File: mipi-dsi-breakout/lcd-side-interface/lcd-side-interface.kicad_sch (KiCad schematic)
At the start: 5 parts

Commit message: Add symbols for the rest of the lcd screens.
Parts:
- removed S1: ~, symbol project:et060hd02_t_dsi_conn
- removed U1: ~, symbol project:tst043wvbi_130c_ctp_conn
- removed U2: ~, symbol project:et050fw04_t_dsi_conn
- removed X1: ~, symbol project:mipi_breakout_header_conn
- removed Y1: ~, symbol project:tst043wvbi_130c_dsi_conn

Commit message: Layout schematic for lcd side interface.
Also change most pins on the mipi 20 pin header interface connector to
bidirectional to avoid ERC headache.
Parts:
- added H1: MountingHole_Pad, symbol Mechanical:MountingHole_Pad
- added X1: ~, symbol project:mipi_breakout_header_conn
- added et050fw04_t_dsi1: ~, symbol project:et050fw04_t_dsi_conn
- added et060hd02_t_dsi1: ~, symbol project:et060hd02_t_dsi_conn
- added tst043wvbi_130c_ctp1: ~, symbol project:tst043wvbi_130c_ctp_conn
- added tst043wvbi_130c_dsi1: ~, symbol project:tst043wvbi_130c_dsi_conn
- added tst050hdbs_80c_ctp1: ~, symbol project:tst050hdbs_80c_ctp_conn
- added tst050hdbs_80c_dsi1: ~, symbol project:tst050hdbs_80c_dsi_conn
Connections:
- new net +1V8: X1.2 (VCC1.8), et050fw04_t_dsi1.18 (IOVCC_1.8V), et050fw04_t_dsi1.19 (IOVCC_1.8V), et060hd02_t_dsi1.18 (IOVCC), tst043wvbi_130c_dsi1.7 (IOVCC), tst050hdbs_80c_ctp1.2 (VDDIO), tst050hdbs_80c_dsi1.8 (IOVCC)
- new net DSI_0_N: X1.11 (DSI_0_N), et050fw04_t_dsi1.3 (MIPI_0N), et060hd02_t_dsi1.13 (TD0N), tst043wvbi_130c_dsi1.15 (MIPI_D0_N), tst050hdbs_80c_dsi1.13 (D0N)
- new net DSI_0_P: X1.12 (DSI_0_P), et050fw04_t_dsi1.2 (MIPI_0P), et060hd02_t_dsi1.14 (TD0P), tst043wvbi_130c_dsi1.16 (MIPI_D0_P), tst050hdbs_80c_dsi1.14 (D0P)
- new net DSI_1_N: X1.13 (DSI_1_N), et050fw04_t_dsi1.6 (MIPI_1N), et060hd02_t_dsi1.10 (TD1N), tst043wvbi_130c_dsi1.13 (MIPI_D1_N), tst050hdbs_80c_dsi1.16 (D1N)
- new net DSI_1_P: X1.14 (DSI_1_P), et050fw04_t_dsi1.5 (MIPI_1P), et060hd02_t_dsi1.11 (TD1P), tst043wvbi_130c_dsi1.12 (MIPI_D1_P), tst050hdbs_80c_dsi1.17 (D1P)
- new net DSI_2_N: X1.17 (DSI_2_N), et060hd02_t_dsi1.4 (TD2N), tst050hdbs_80c_dsi1.22 (D2N)
- new net DSI_2_P: X1.18 (DSI_2_P), et060hd02_t_dsi1.5 (TD2P), tst050hdbs_80c_dsi1.23 (D2P)
- new net DSI_3_N: X1.19 (DSI_3_N), et060hd02_t_dsi1.1 (TD3N), tst050hdbs_80c_dsi1.25 (D3N)
- new net DSI_3_P: X1.20 (DSI_3_P), et060hd02_t_dsi1.2 (TD3P), tst050hdbs_80c_dsi1.26 (D3P)
- new net DSI_CLK_N: X1.15 (DSI_CLK_N), et050fw04_t_dsi1.9 (MIPI_CKN), et060hd02_t_dsi1.7 (TCN), tst043wvbi_130c_dsi1.19 (MIPI_CLK_N), tst050hdbs_80c_dsi1.19 (CLKN)
- new net DSI_CLK_P: X1.16 (DSI_CLK_P), et050fw04_t_dsi1.8 (MIPI_CKP), et060hd02_t_dsi1.8 (TCP), tst043wvbi_130c_dsi1.18 (MIPI_CLK_P), tst050hdbs_80c_dsi1.20 (CLKP)
- new net GND: H1.1, X1.3 (GND), et050fw04_t_dsi1.1 (GND), et050fw04_t_dsi1.10 (GND), et050fw04_t_dsi1.13 (GND), et050fw04_t_dsi1.16 (GND), et050fw04_t_dsi1.17 (GND), et050fw04_t_dsi1.27 (GND), et050fw04_t_dsi1.30 (GND), et050fw04_t_dsi1.32 (GND), et050fw04_t_dsi1.33 (GND), et050fw04_t_dsi1.37 (GND), et050fw04_t_dsi1.4 (GND), et050fw04_t_dsi1.7 (GND), et060hd02_t_dsi1.12 (GND), et060hd02_t_dsi1.15 (GND), et060hd02_t_dsi1.19 (GND), et060hd02_t_dsi1.3 (GND), et060hd02_t_dsi1.6 (GND), et060hd02_t_dsi1.9 (GND), tst043wvbi_130c_ctp1.4 (GND), tst043wvbi_130c_ctp1.8 (GND), tst043wvbi_130c_ctp1.9 (GND), tst043wvbi_130c_dsi1.11 (GND), tst043wvbi_130c_dsi1.14 (GND), tst043wvbi_130c_dsi1.17 (GND), tst043wvbi_130c_dsi1.8 (GND), tst050hdbs_80c_ctp1.1 (GND), tst050hdbs_80c_ctp1.8 (GND), tst050hdbs_80c_dsi1.12 (GND), tst050hdbs_80c_dsi1.15 (GND), tst050hdbs_80c_dsi1.18 (GND), tst050hdbs_80c_dsi1.21 (GND), tst050hdbs_80c_dsi1.24 (GND), tst050hdbs_80c_dsi1.27 (GND), tst050hdbs_80c_dsi1.28 (GND), tst050hdbs_80c_dsi1.6 (GND)
- new net INT: X1.5 (INTERRUPT), tst043wvbi_130c_ctp1.5 (Interrupt), tst050hdbs_80c_ctp1.6 (INT)
- new net LED_A: X1.9 (LED_A), et050fw04_t_dsi1.35 (LED_A), et050fw04_t_dsi1.36 (LED_A), et060hd02_t_dsi1.24 (LEDA), et060hd02_t_dsi1.25 (LEDA), tst043wvbi_130c_dsi1.1 (LED_A), tst043wvbi_130c_dsi1.2 (LED_A), tst050hdbs_80c_dsi1.2 (LEDA), tst050hdbs_80c_dsi1.3 (LEDA)
- new net LED_K: X1.10 (LED_K), et050fw04_t_dsi1.28 (LED_K), et050fw04_t_dsi1.29 (LED_K), et060hd02_t_dsi1.21 (LEDK), et060hd02_t_dsi1.22 (LEDK), tst043wvbi_130c_dsi1.3 (LED_K), tst043wvbi_130c_dsi1.4 (LED_K), tst050hdbs_80c_dsi1.4 (LEDK), tst050hdbs_80c_dsi1.5 (LEDK)
- new net RESET: X1.4 (RESET_N), et050fw04_t_dsi1.24 (RESET), et060hd02_t_dsi1.16 (RESET), tst043wvbi_130c_ctp1.3 (Reset), tst043wvbi_130c_dsi1.10 (LCD_RST_N), tst050hdbs_80c_ctp1.7 (RST), tst050hdbs_80c_dsi1.11 (RESET_B)
- new net SCL: X1.7 (SCL), tst043wvbi_130c_ctp1.7 (SCL), tst050hdbs_80c_ctp1.4 (SCL)
- new net SDA: X1.8 (SDA), tst043wvbi_130c_ctp1.6 (SDA), tst050hdbs_80c_ctp1.5 (SDA)
- new net TE_O: X1.6 (TE_O), et050fw04_t_dsi1.20 (TE), tst043wvbi_130c_dsi1.9 (LCD_TEO), tst050hdbs_80c_dsi1.10 (TE)
- new net VCC: X1.1 (VCC), et050fw04_t_dsi1.38 (VCC_2.8V), et050fw04_t_dsi1.39 (VCC_2.8V), et060hd02_t_dsi1.17 (VCC), tst043wvbi_130c_ctp1.10 (VDD), tst043wvbi_130c_dsi1.6 (VCC), tst050hdbs_80c_ctp1.3 (VDD), tst050hdbs_80c_dsi1.7 (VCC2.8V)
- no-connect marks 0 -> 2
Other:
- note added: "Exposed ground pad (no through hole) for grounding SUS cable stiffeners. (This is meant to be connected using flexible conductive tape.)"

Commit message: Hook up step models to footprints.
Also add new footprint for sus grounding pad.
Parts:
- H1: footprint (none) -> project:sus-grounding-pad
- X1: footprint (none) -> Connector_PinHeader_2.54mm:PinHeader_1x20_P2.54mm_Horizontal
- et050fw04_t_dsi1: footprint (none) -> project:Cvilux_CF4240FH0R0-05-NH_40pos-0.5mm-zif
- et060hd02_t_dsi1: footprint (none) -> project:Cvilux_CF5825DH0RA-NH_25pos-0.3mm-zif
- tst043wvbi_130c_ctp1: footprint (none) -> project:TE_1-2328702-0_10pos-0.5mm-zif
- tst043wvbi_130c_dsi1: footprint (none) -> project:Cvilux_CF4220FH0R0-05-NH_20pos-0.5mm-zif
- tst050hdbs_80c_ctp1: footprint (none) -> project:TE_2328702_8pos-0.5mm-zif
- tst050hdbs_80c_dsi1: footprint (none) -> project:Cvilux_CF4230FH0R0-05-NH_30pos-0.5mm-zif
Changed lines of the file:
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@@
 			)
 		)
-		(property "Footprint" ""
+		(property "Footprint" "project:sus-grounding-pad"
 			(at 193.04 144.78 0)
 			(effects
@@
 			)
 		)
-		(property "Footprint" ""
+		(property "Footprint" "project:TE_2328702_8pos-0.5mm-zif"
 			(at 113.03 63.5 0)
 			(effects
@@
 			)
 		)
-		(property "Footprint" ""
+		(property "Footprint" "project:TE_1-2328702-0_10pos-0.5mm-zif"
 			(at 113.03 106.68 0)
 			(effects
@@
 			)
 		)
-		(property "Footprint" ""
+		(property "Footprint" "project:Cvilux_CF4230FH0R0-05-NH_30pos-0.5mm-zif"
 			(at 168.91 86.36 0)
 			(effects
@@
 			)
 		)
-		(property "Footprint" ""
+		(property "Footprint" "project:Cvilux_CF5825DH0RA-NH_25pos-0.3mm-zif"
 			(at 80.01 86.36 0)
 			(effects
@@
 			)
 		)
-		(property "Footprint" ""
+		(property "Footprint" "Connector_PinHeader_2.54mm:PinHeader_1x20_P2.54mm_Horizontal"
 			(at 146.05 157.48 0)
 			(effects
@@
 			)
 		)
-		(property "Footprint" ""
+		(property "Footprint" "project:Cvilux_CF4240FH0R0-05-NH_40pos-0.5mm-zif"
 			(at 219.71 80.01 0)
 			(effects
@@
 			)
 		)
-		(property "Footprint" ""
+		(property "Footprint" "project:Cvilux_CF4220FH0R0-05-NH_20pos-0.5mm-zif"
 			(at 83.82 158.75 0)
 			(effects

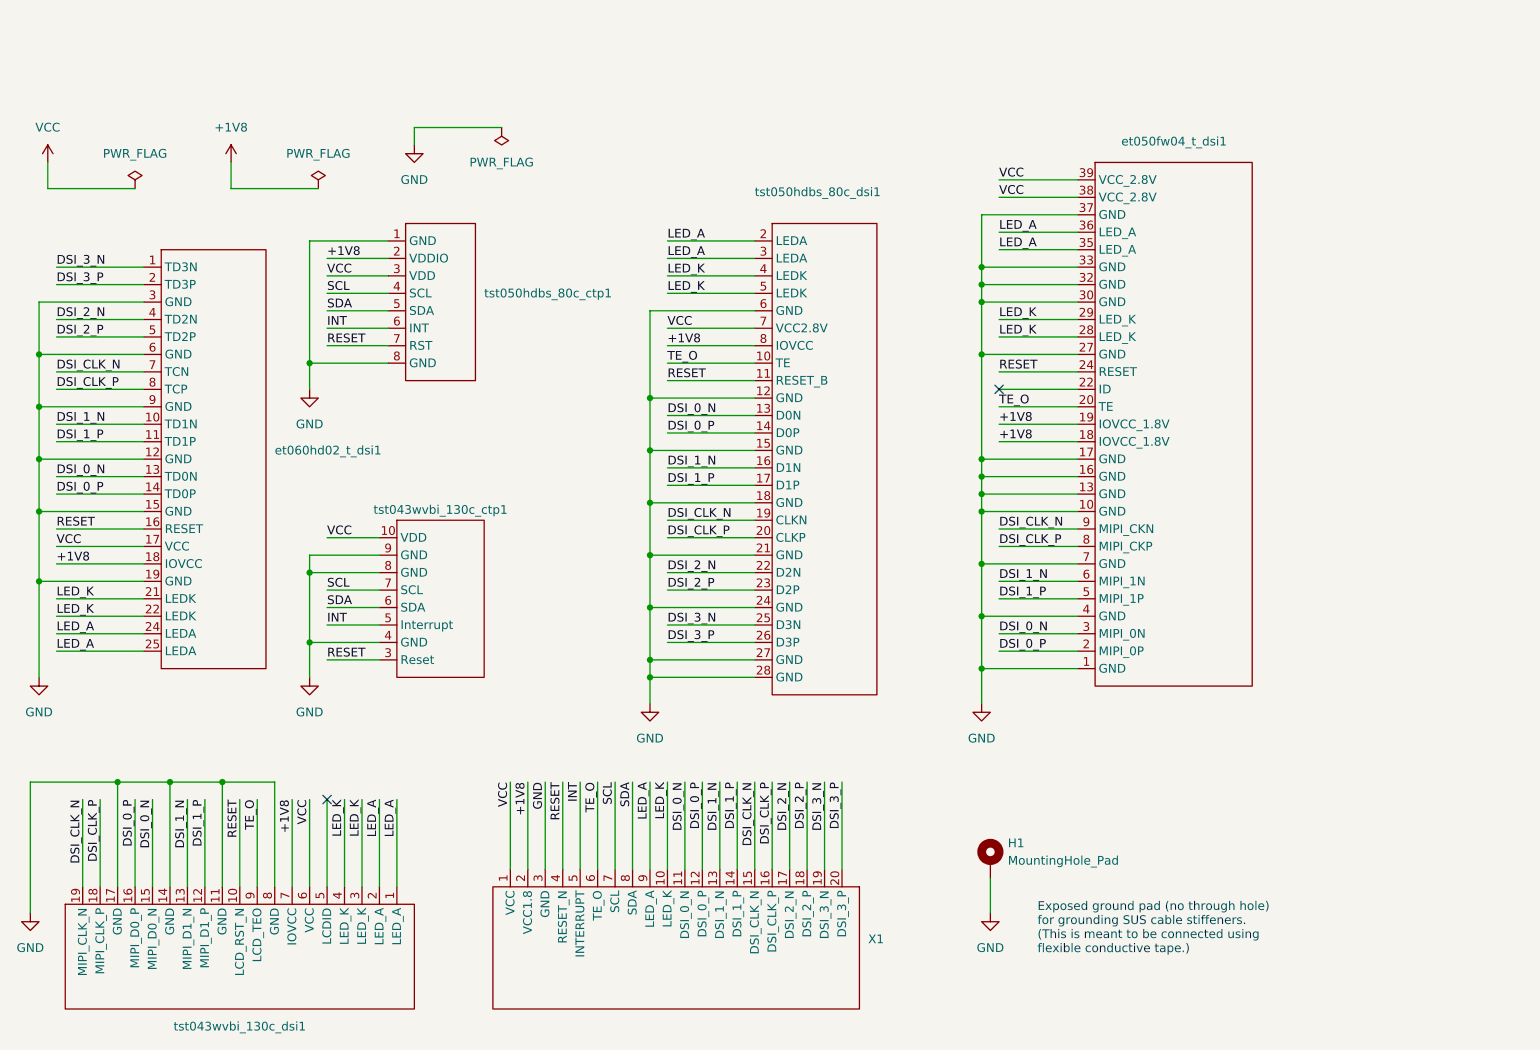
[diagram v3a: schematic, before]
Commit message: Fill out lcd side interface + double check errors.
* Flip orientation of most connectors to match orientation of real world
  parts.

* Added NC pins to symbol so they are matched up to the footprints.

* Added a RESET_FAILSAFE solder bridge that can be cut in the case that
  the CTP touch screen resets aren't active low and the DSI resets are.

* Double check pin ordering and reset signals.
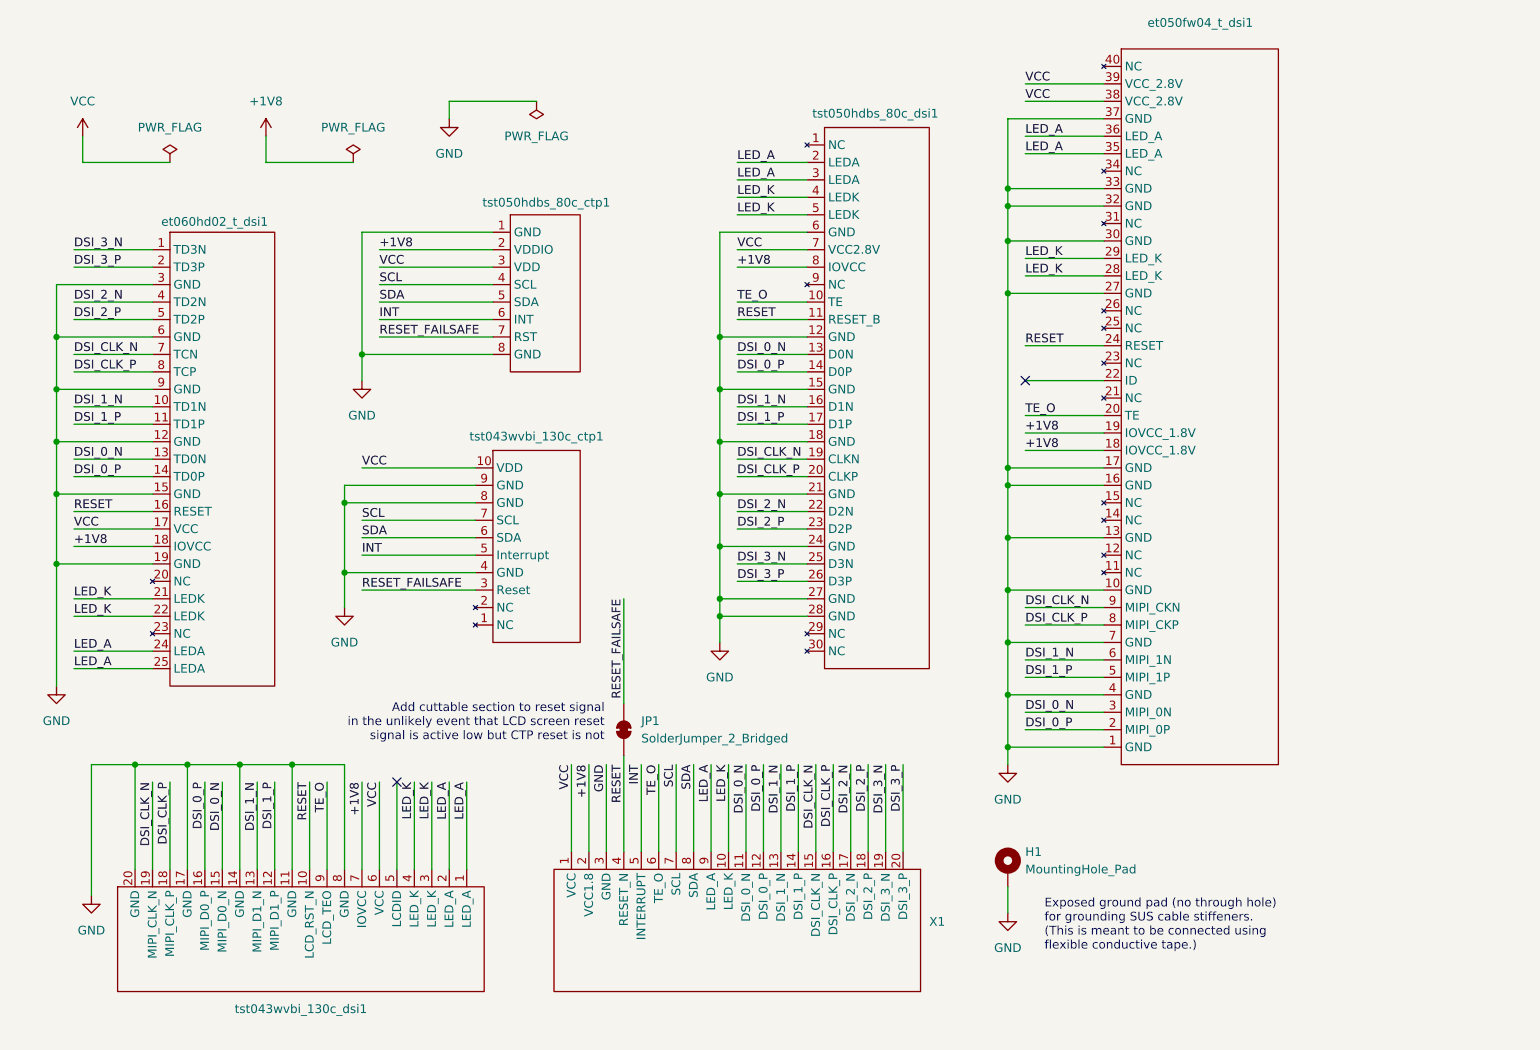
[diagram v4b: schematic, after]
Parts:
- added JP1: SolderJumper_2_Bridged, Jumper:SolderJumper-2_P1.3mm_Bridged_Pad1.0x1.5mm, symbol Jumper:SolderJumper_2_Bridged
- X1: footprint Connector_PinHeader_2.54mm:PinHeader_1x20_P2.54mm_Horizontal -> Connector_PinHeader_2.54mm:PinHeader_1x20_P2.54mm_Vertical
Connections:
- net GND: now also tst043wvbi_130c_dsi1.20 (GND)
- net RESET: now also JP1.1 (A); no longer tst043wvbi_130c_ctp1.3 (Reset), tst050hdbs_80c_ctp1.7 (RST)
- new net RESET_FAILSAFE: JP1.2 (B), tst043wvbi_130c_ctp1.3 (Reset), tst050hdbs_80c_ctp1.7 (RST)
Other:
- note added: "Add cuttable section to reset signal in the unlikely event that LCD screen reset signal is active low but CTP reset is not"
- moved on the sheet: H1, X1, tst050hdbs_80c_ctp1
